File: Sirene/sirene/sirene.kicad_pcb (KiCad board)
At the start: 2 copper layers, 19 parts, among them Q1 BC557, Q2 BC547, Q3 BC557, Q4 BC557, Q5 TIP42

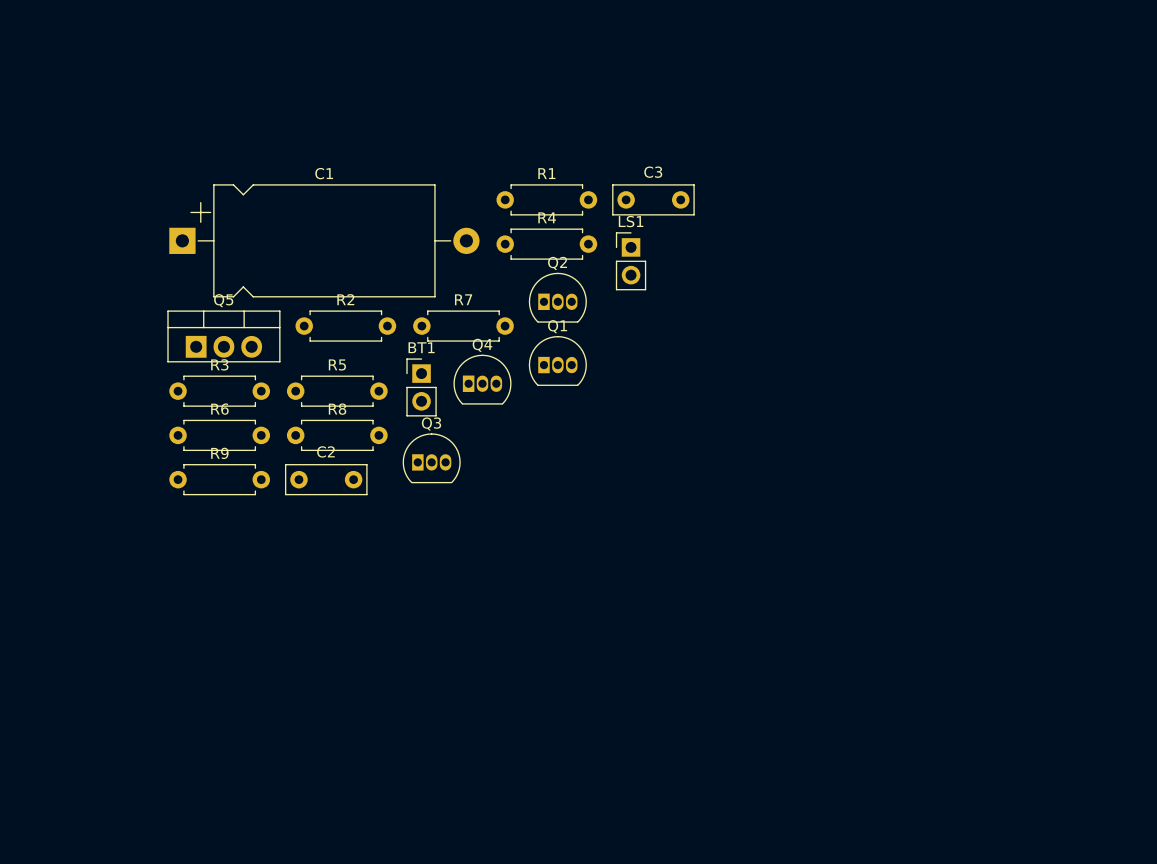
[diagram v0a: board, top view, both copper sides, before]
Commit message: Sirene PCB layout.
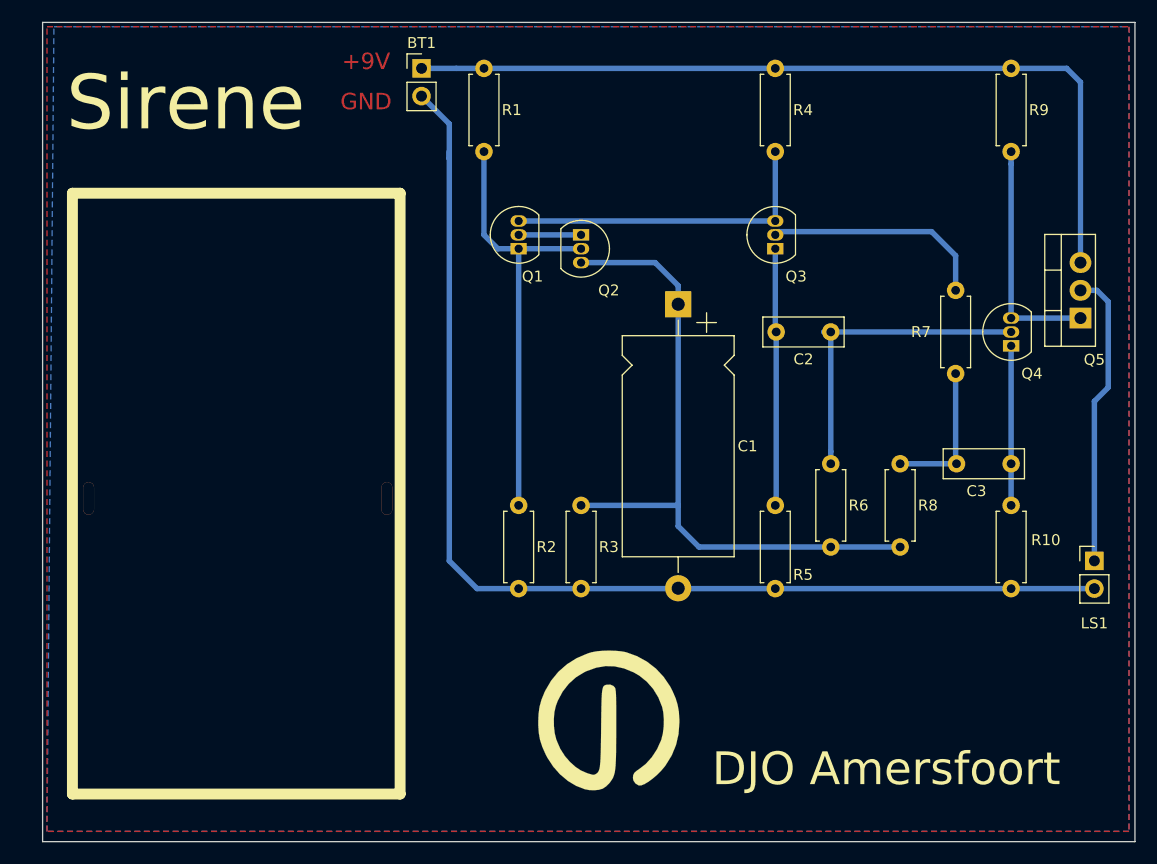
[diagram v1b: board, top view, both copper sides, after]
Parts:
- added G***: LOGO, DJO logo:DJO logo 16mm, F.Cu at (76.8, 88.9)
- added R10: 100R, Resistor_THT:R_Axial_DIN0207_L6.3mm_D2.5mm_P7.62mm_Horizontal, F.Cu at (113.7, 69.2)
- added REF**: Tiewrap hole, DJO_mechanical:Tiewrap hole, F.Cu at (56.5, 68.6)
- added REF**: Tiewrap hole, DJO_mechanical:Tiewrap hole, F.Cu at (29.2, 68.6)
- R7: value 10k -> 0R
- R9: value 100R -> 10k
- moved R9 85.1 mm to (113.7, 29.2), turned to 270 degrees
- moved Q5 81.0 mm to (120.0, 52.1), turned to 90 degrees
- moved R6 59.8 mm to (97.2, 65.4), turned to 270 degrees
- moved R8 55.4 mm to (103.5, 65.4), turned to 270 degrees
- moved LS1 51.2 mm to (121.3, 74.3)
- moved C2 50.5 mm to (97.2, 53.3), turned to 180 degrees
- moved Q4 49.8 mm to (113.7, 54.6), turned to 90 degrees
- moved R7 49.1 mm to (108.6, 57.1), turned to 90 degrees
- moved C1 45.8 mm to (83.2, 50.8), turned to 270 degrees
- moved R5 45.1 mm to (92.1, 69.2), turned to 270 degrees
- moved C3 42.7 mm to (113.7, 65.4), turned to 180 degrees
- moved R3 38.3 mm to (74.3, 69.2), turned to 270 degrees
- moved Q3 38.1 mm to (92.1, 45.7), turned to 90 degrees
- moved R4 29.5 mm to (92.1, 29.2), turned to 270 degrees
- moved BT1 27.9 mm to (59.7, 29.2)
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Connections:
- BT1 pad 2: Net-(BT1-Pad2) -> GND
- C1 pad 2: Net-(BT1-Pad2) -> GND
- LS1 pad 2: Net-(BT1-Pad2) -> GND
- Q3 pad 2: Net-(C3-Pad2) -> Net-(Q3-Pad2)
- R2 pad 2: Net-(BT1-Pad2) -> GND
- R3 pad 2: Net-(BT1-Pad2) -> GND
- R5 pad 2: Net-(BT1-Pad2) -> GND
- R7 pad 2: Net-(C1-Pad1) -> Net-(Q3-Pad2)
- R8 pad 1: Net-(BT1-Pad1) -> Net-(C3-Pad2)
- R8 pad 2: Net-(Q4-Pad3) -> Net-(C1-Pad1)
- R9 pad 1: Net-(C3-Pad1) -> Net-(BT1-Pad1)
- R9 pad 2: Net-(BT1-Pad2) -> Net-(Q4-Pad3)
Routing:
- net GND: track 0.00 -> 104.3 mm
- net Net-(BT1-Pad1): track 0.00 -> 77.4 mm
- net Net-(C1-Pad1): track 0.00 -> 61.8 mm
- net Net-(Q1-Pad1): track 0.00 -> 40.5 mm
- net Net-(Q1-Pad3): track 0.00 -> 30.5 mm
- net Net-(C2-Pad1): track 0.00 -> 29.8 mm
- net Net-(LS1-Pad1): track 0.00 -> 27.2 mm
- net Net-(C2-Pad2): track 0.00 -> 23.6 mm
- net Net-(Q4-Pad3): track 0.00 -> 21.6 mm
- net Net-(Q3-Pad2): track 0.00 -> 20.7 mm
- net Net-(C3-Pad1): track 0.00 -> 14.6 mm
- net Net-(C3-Pad2): track 0.00 -> 13.4 mm
- net Net-(Q1-Pad2): track 0.00 -> 5.72 mm
- added copper zone on F.Cu, net (none)
- added copper zone on B.Cu, net GND
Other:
- board outline added: 100 x 75 mm
- rule via_min_drill: 0.3 -> 0.25
- board text added: "+9V"
- board text added: "BT1: Batterij 9V"
- board text added: "Batterij"
- board text added: "C1: 220uF"
- board text added: "C2, C3: 47nF"
- board text added: "Condensatoren"
- board text added: "DJO Amersfoort"
- board text added: "GND"
- board text added: "LS1: Luidspreker 8 Ohm"
- board text added: "Luidspreker"
- board text added: "Q1, Q3, Q4: BC557"
- board text added: "Q2: BC547"
- board text added: "Q5: TIP42"
- board text added: "R1, R2, R5, R6, R8, R9: 10K"
- board text added: "R3: 2k7"
- board text added: "R4, R10: 100 Ohm"
- board text added: "R7: 0 Ohm"
- board text added: "Sirene"
- board text added: "Transistoren"
- board text added: "Weerstanden"
